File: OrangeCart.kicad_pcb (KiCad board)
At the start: 4 copper layers, 62 x 60 mm, 131 parts, among them J1 Conn_02x11_Odd_Even, J2 UART, J3 USB_B_Mini, J4 MicroSd, J6 JTAG, SW1 SW_Push, U1 FAN53541, U10 NCP115-2.5, U11 74AHCV17A, U12 74LVC3G17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

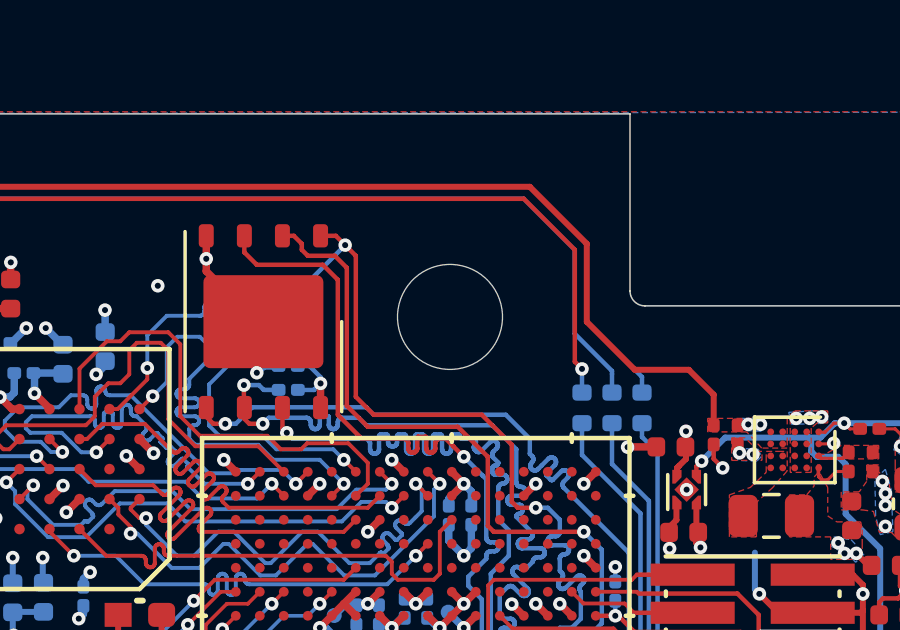
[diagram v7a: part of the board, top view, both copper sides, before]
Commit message: Adjust screw hole position
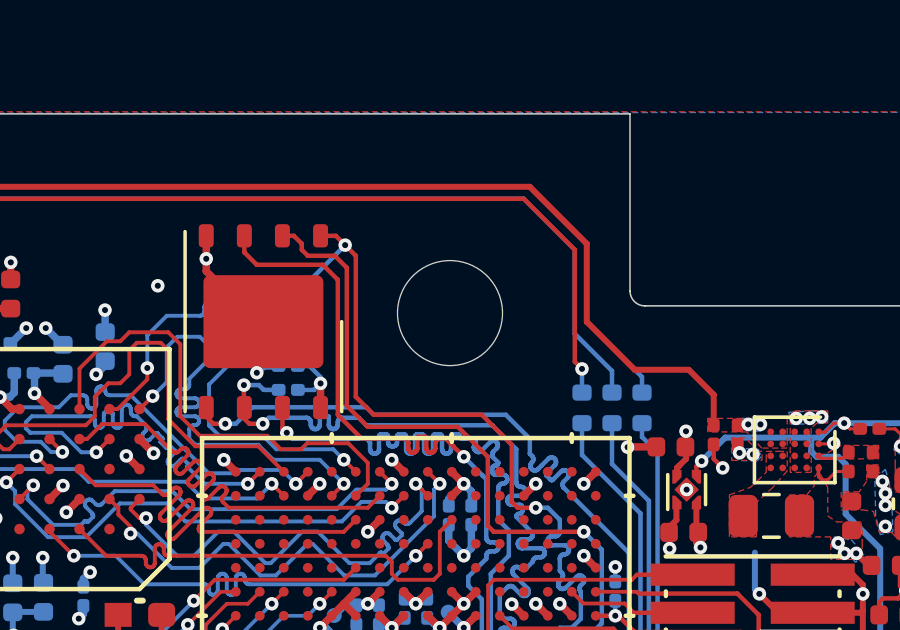
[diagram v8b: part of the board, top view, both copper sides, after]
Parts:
- moved CART1 0.13 mm to (80.0, 84.7)
